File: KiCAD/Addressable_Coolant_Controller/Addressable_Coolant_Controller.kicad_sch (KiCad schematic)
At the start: 3 parts, among them J1 XW4M-12D2-H1DA, J2 XW4M-02D1-H1DA, J3 XW4M-12D2-H1DA

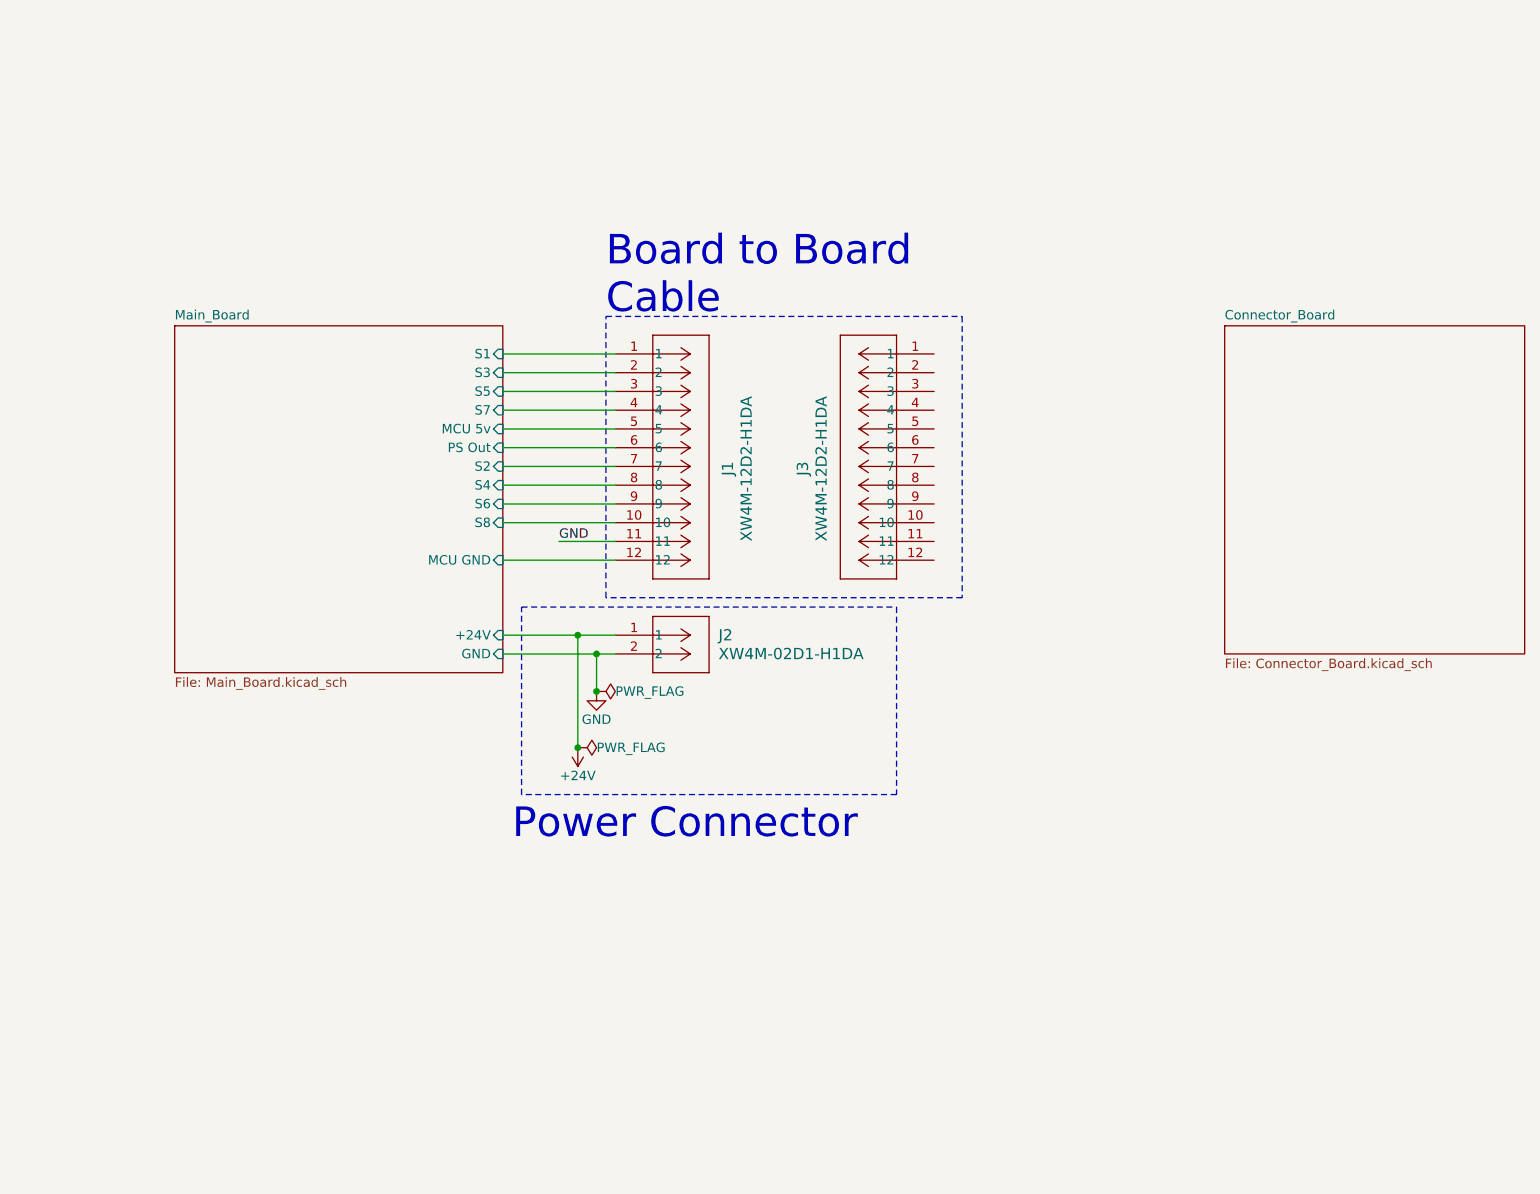
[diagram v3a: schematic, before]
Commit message: Fixed broken netclasses, removed voltage divider circuit
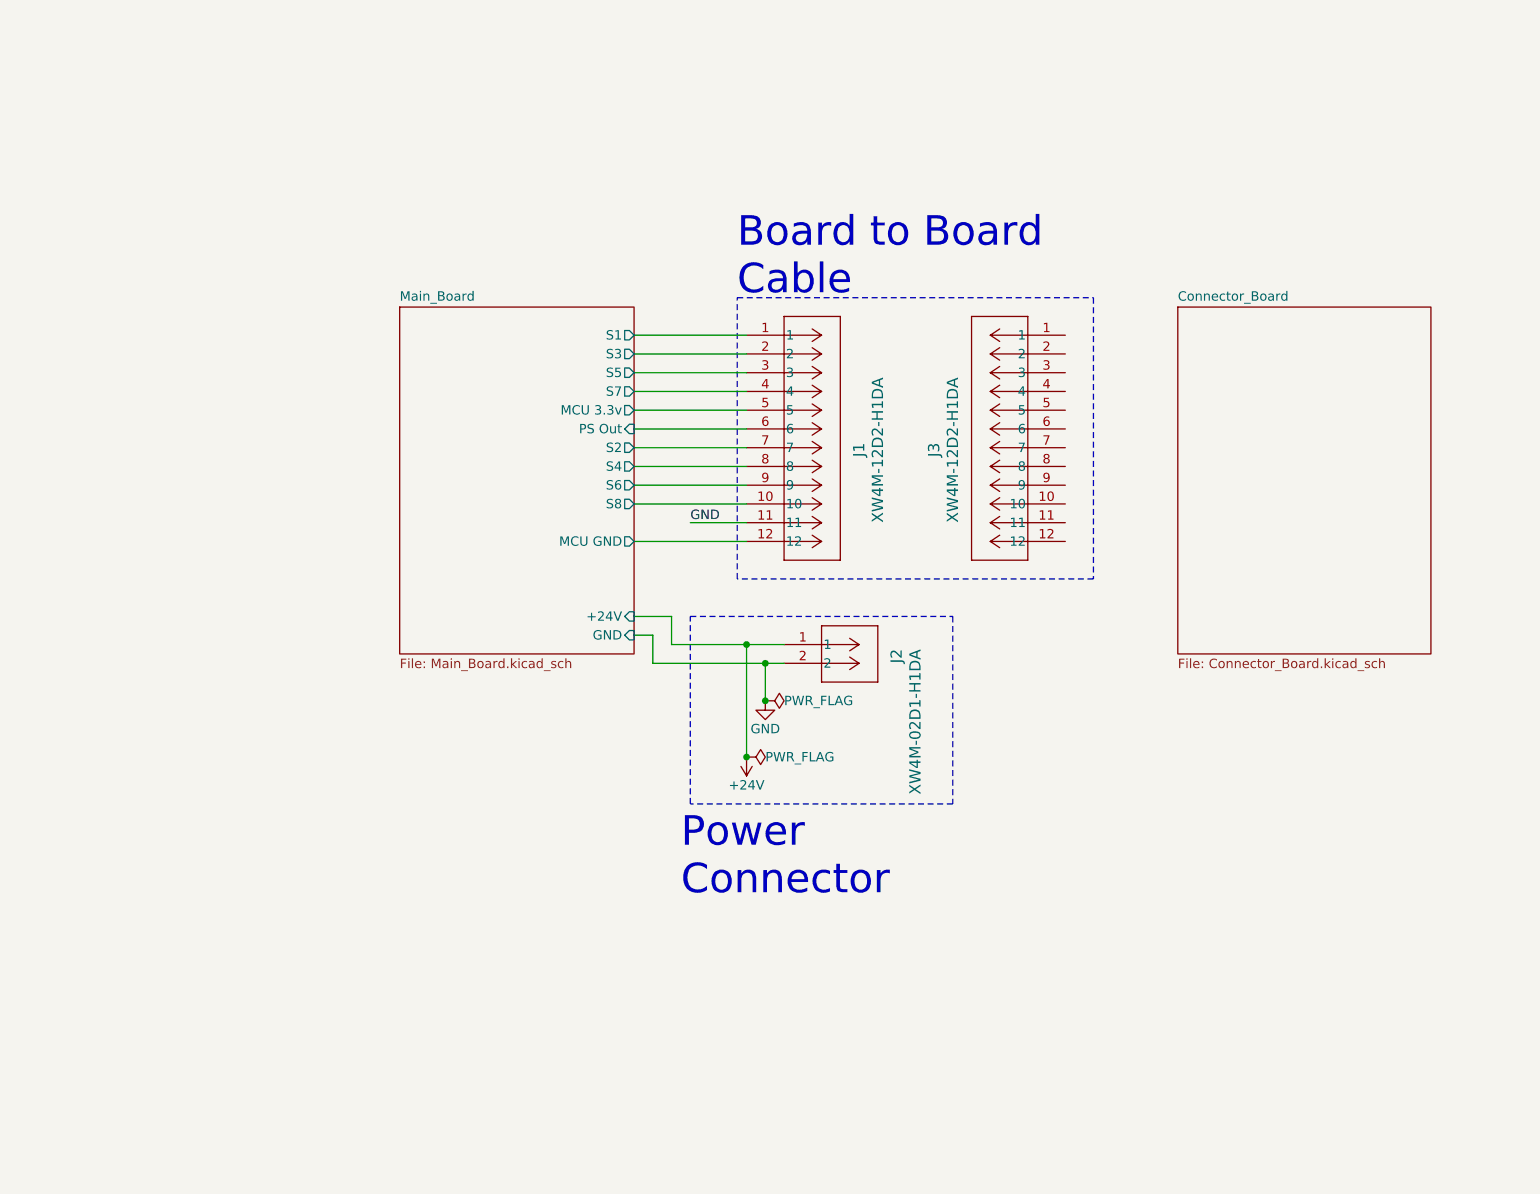
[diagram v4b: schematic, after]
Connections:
- net Main_Board/MCU 5v renamed Main_Board/MCU 3.3v
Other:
- sheet Main_Board ports: added MCU 3.3v; removed MCU 5v
- company: (none) -> Warner Consulting Inc.
- title: (none) -> Addressable Coolant Controller
- moved on the sheet: J1, J2, J3

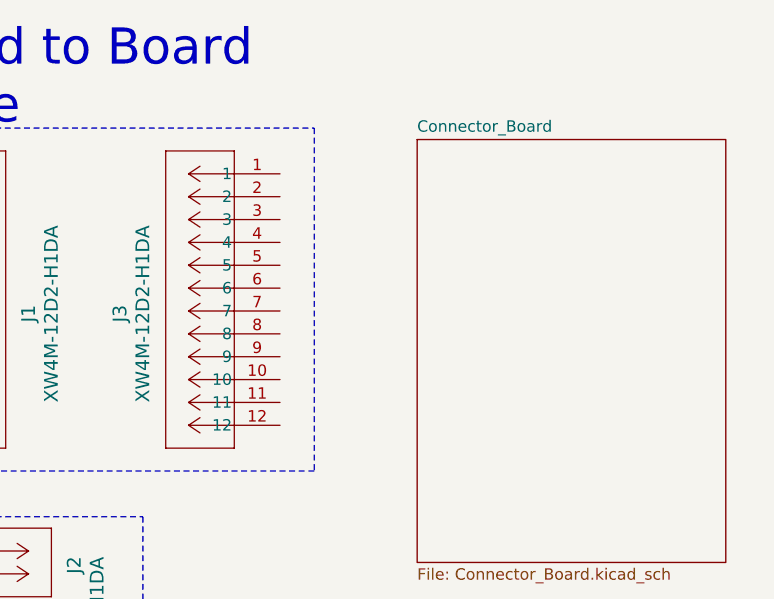
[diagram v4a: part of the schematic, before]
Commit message: Added hierarchical labels to connector board
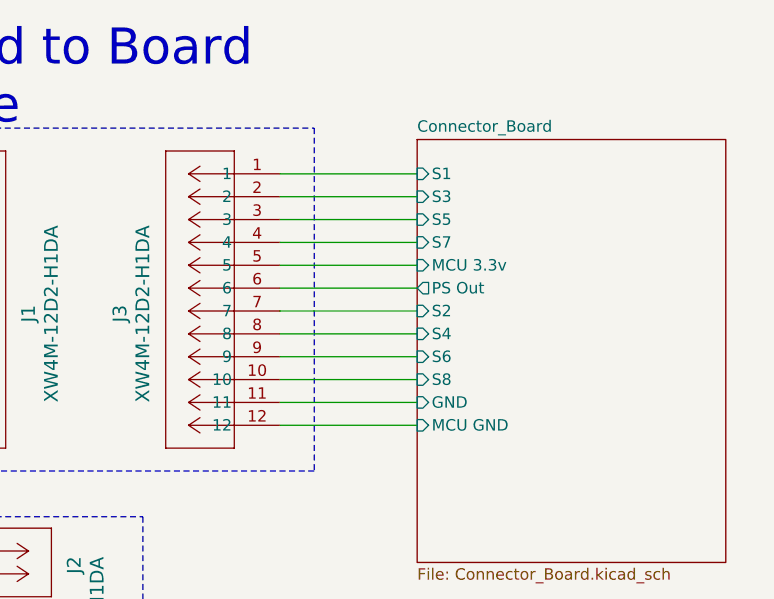
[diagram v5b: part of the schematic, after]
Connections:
- net Connector_Board/S1: now reaches J3.1
- net Connector_Board/S8: now reaches J3.10
- net Connector_Board/GND: now reaches J3.11
- net Connector_Board/MCU GND: now reaches J3.12
- net Connector_Board/S3: now reaches J3.2
- net Connector_Board/S5: now reaches J3.3
- net Connector_Board/S7: now reaches J3.4
- net Connector_Board/MCU 3.3v: now reaches J3.5
- net Connector_Board/PS Out: now reaches J3.6
- net Connector_Board/S2: now reaches J3.7
- net Connector_Board/S4: now reaches J3.8
- net Connector_Board/S6: now reaches J3.9
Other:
- sheet Connector_Board ports: added GND, MCU 3.3v, MCU GND, PS Out, S1, S2, S3, S4, S5, S6, S7, S8; removed none
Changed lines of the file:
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@@
   (junction (at 127 111.76) (diameter 0) (color 0 0 0 0)
   )
+  (wire (pts (xy 170.18 90.17) (xy 185.42 90.17))
+    (stroke (width 0) (type default))
+  )
+  (wire (pts (xy 170.18 85.09) (xy 185.42 85.09))
+    (stroke (width 0) (type default))
+  )
   (wire (pts (xy 111.76 92.71) (xy 127 92.71))
     (stroke (width 0) (type default))
@@
     (stroke (width 0) (type default))
   )
+  (wire (pts (xy 170.18 77.47) (xy 185.42 77.47))
+    (stroke (width 0) (type default))
+  )
   (wire (pts (xy 129.54 119.38) (xy 129.54 114.3))
     (stroke (width 0) (type default))
@@
     (stroke (width 0) (type default))
   )
+  (wire (pts (xy 170.18 97.79) (xy 185.42 97.79))
+    (stroke (width 0) (type default))
+  )
+  (wire (pts (xy 170.18 74.93) (xy 185.42 74.93))
+    (stroke (width 0) (type default))
+  )
   (wire (pts (xy 116.84 111.76) (xy 116.84 107.95))
     (stroke (width 0) (type default))
   )
+  (wire (pts (xy 170.18 69.85) (xy 185.42 69.85))
+    (stroke (width 0) (type default))
+  )
   (wire (pts (xy 111.76 74.93) (xy 127 74.93))
     (stroke (width 0) (type default))
@@
     (stroke (width 0) (type default))
   )
+  (wire (pts (xy 170.18 87.63) (xy 185.42 87.63))
+    (stroke (width 0) (type default))
+  )
+  (wire (pts (xy 170.18 92.71) (xy 185.42 92.71))
+    (stroke (width 0) (type default))
+  )
   (wire (pts (xy 111.76 82.55) (xy 127 82.55))
     (stroke (width 0) (type default))
   )
+  (wire (pts (xy 170.18 82.55) (xy 185.42 82.55))
+    (stroke (width 0) (type default))
+  )
   (wire (pts (xy 114.3 110.49) (xy 114.3 114.3))
     (stroke (width 0) (type default))
   )
+  (wire (pts (xy 170.18 95.25) (xy 185.42 95.25))
+    (stroke (width 0) (type default))
+  )
   (wire (pts (xy 116.84 111.76) (xy 127 111.76))
     (stroke (width 0) (type default))
@@
   )
   (wire (pts (xy 111.76 90.17) (xy 127 90.17))
+    (stroke (width 0) (type default))
+  )
+  (wire (pts (xy 170.18 72.39) (xy 185.42 72.39))
+    (stroke (width 0) (type default))
+  )
+  (wire (pts (xy 170.18 80.01) (xy 185.42 80.01))
     (stroke (width 0) (type default))
   )
@@
       (effects (font (size 1.27 1.27)) (justify left top))
     )
+    (pin "S1" input (at 185.42 69.85 180)
+      (effects (font (size 1.27 1.27)) (justify left))
+    )
+    (pin "S2" input (at 185.42 85.09 180)
+      (effects (font (size 1.27 1.27)) (justify left))
+    )
+    (pin "S3" input (at 185.42 72.39 180)
+      (effects (font (size 1.27 1.27)) (justify left))
+    )
+    (pin "S4" input (at 185.42 87.63 180)
+      (effects (font (size 1.27 1.27)) (justify left))
+    )
+    (pin "S5" input (at 185.42 74.93 180)
+      (effects (font (size 1.27 1.27)) (justify left))
+    )
+    (pin "S6" input (at 185.42 90.17 180)
+      (effects (font (size 1.27 1.27)) (justify left))
+    )
+    (pin "S7" input (at 185.42 77.47 180)
+      (effects (font (size 1.27 1.27)) (justify left))
+    )
+    (pin "S8" input (at 185.42 92.71 180)
+      (effects (font (size 1.27 1.27)) (justify left))
+    )
+    (pin "MCU 3.3v" input (at 185.42 80.01 180)
+      (effects (font (size 1.27 1.27)) (justify left))
+    )
+    (pin "MCU GND" input (at 185.42 97.79 180)
+      (effects (font (size 1.27 1.27)) (justify left))
+    )
+    (pin "PS Out" output (at 185.42 82.55 180)
+      (effects (font (size 1.27 1.27)) (justify left))
+    )
+    (pin "GND" input (at 185.42 95.25 180)
+      (effects (font (size 1.27 1.27)) (justify left))
+    )
     (instances

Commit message: Routed connector PCB and fixed components designators
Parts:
- renumbered J1 to J10, J3 to J11, J2 to J12
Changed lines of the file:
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@@
   (symbol (lib_id "xw4m-12d2-h1da:XW4M-12D2-H1DA") (at 170.18 69.85 0) (mirror y) (unit 1)
     (in_bom yes) (on_board yes) (dnp no)
-    (property "Reference" "J3" (at 152.4 86.36 90)
+    (property "Reference" "J11" (at 152.4 86.36 90)
       (effects (font (size 1.524 1.524)) (justify left))
     )
@@
       (project "Addressable_Coolant_Controller"
         (path "/603d0a2e-fca7-40af-8fa8-51b59d823d4d"
-          (reference "J3") (unit 1)
+          (reference "J11") (unit 1)
         )
       )
@@
   (symbol (lib_id "xw4m-12d2-h1da:XW4M-12D2-H1DA") (at 127 69.85 0) (unit 1)
     (in_bom yes) (on_board yes) (dnp no)
-    (property "Reference" "J1" (at 142.24 86.36 90)
+    (property "Reference" "J10" (at 142.24 86.36 90)
       (effects (font (size 1.524 1.524)) (justify left))
     )
@@
       (project "Addressable_Coolant_Controller"
         (path "/603d0a2e-fca7-40af-8fa8-51b59d823d4d"
-          (reference "J1") (unit 1)
+          (reference "J10") (unit 1)
         )
       )
@@
   (symbol (lib_id "xw4m-02d1-h1da:XW4M-02D1-H1DA") (at 132.08 111.76 0) (unit 1)
     (in_bom yes) (on_board yes) (dnp no)
-    (property "Reference" "J2" (at 147.32 114.3 90)
+    (property "Reference" "J12" (at 147.32 114.3 90)
       (effects (font (size 1.524 1.524)) (justify left))
     )
@@
       (project "Addressable_Coolant_Controller"
         (path "/603d0a2e-fca7-40af-8fa8-51b59d823d4d"
-          (reference "J2") (unit 1)
+          (reference "J12") (unit 1)
         )
       )
